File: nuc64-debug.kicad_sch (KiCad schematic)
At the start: 12 parts, among them J1 SWD, J2 POW, SW1 BOOT, SW2 RST

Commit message: Fixed trace width
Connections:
- net VBUS: now reaches DBG1.9 (Pin_9), J2.3 (Pin_3)
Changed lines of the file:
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@@
+	)
+	(junction
+		(at 152.4 35.56)
+		(diameter 0)
+		(color 0 0 0 0)
 	)
 	(junction
@@
 	(wire
 		(pts
+			(xy 171.45 35.56) (xy 171.45 27.94)
+		)
+		(stroke
+			(width 0)
+			(type default)
+		)
+	)
+	(wire
+		(pts
 			(xy 154.94 73.66) (xy 154.94 81.28)
 		)
@@
 		(pts
 			(xy 180.34 130.81) (xy 165.1 130.81)
+		)
+		(stroke
+			(width 0)
+			(type default)
+		)
+	)
+	(wire
+		(pts
+			(xy 152.4 35.56) (xy 171.45 35.56)
 		)
 		(stroke
@@
 					(unit 1)
 				)
+			)
+		)
+	)
+	(symbol
+		(lib_id "power:VBUS")
+		(at 171.45 27.94 0)
+		(unit 1)
+		(exclude_from_sim no)
+		(in_bom yes)
+		(on_board yes)
+		(dnp no)
+		(fields_autoplaced yes)
+		(property "Reference" "#PWR02"
+			(at 171.45 31.75 0)
+			(effects
+				(font
+					(size 1.27 1.27)
+				)
+				(hide yes)
+			)
+		)
+		(property "Value" "VBUS"
+			(at 171.45 22.86 0)
+			(effects
+				(font
+					(size 1.27 1.27)
+				)
+			)
+		)
+		(property "Footprint" ""
+			(at 171.45 27.94 0)
+			(effects
+				(font
+					(size 1.27 1.27)
+				)
+				(hide yes)
+			)
+		)
+		(property "Datasheet" ""
+			(at 171.45 27.94 0)
+			(effects
+				(font
+					(size 1.27 1.27)
+				)
+				(hide yes)
+			)
+		)
+		(property "Description" "Power symbol creates a global label with name \"VBUS\""
+			(at 171.45 27.94 0)
+			(effects
+				(font
+					(size 1.27 1.27)
+				)
+				(hide yes)
+			)
+		)
+		(pin "1"
+		)
+		(instances
+			(project ""
+				(path "/12c2bc1e-4869-4a56-bffb-ffa29b2d4bba"
+					(reference "#PWR02")
+					(unit 1)
+				)

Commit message: Shrink
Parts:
- added C3: 10n, Capacitor_SMD:C_0603_1608Metric, symbol Device:C
- added C4: 10µ, Capacitor_SMD:C_0603_1608Metric, symbol Device:C
- added C5: 100n, Capacitor_SMD:C_0603_1608Metric, symbol Device:C
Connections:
- net GND: now also C3.2, C4.2, C5.2
- net VDD: now also C3.1, C4.1, C5.1

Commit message: Added UART LEDs
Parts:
- added D2: RX, LED_SMD:LED_0603_1608Metric, symbol Device:LED
- added D3: TX, LED_SMD:LED_0603_1608Metric, symbol Device:LED
- added R4, R5: 1K, Resistor_SMD:R_0603_1608Metric, symbol Device:R
- added R6, R7: 680, Resistor_SMD:R_0603_1608Metric, symbol Device:R
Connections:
- net VDD: now also D2.2 (A), D3.2 (A), R4.2, R5.2
- net at DBG1.7 (Pin_7), UART1.2 (Pin_2): now also R5.1, R7.2
- net at DBG1.8 (Pin_8), UART1.1 (Pin_1): now also R4.1, R6.2
- new net: D3.1 (K), R7.1
- new net: D2.1 (K), R6.1
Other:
- moved on the sheet: C1, C3, C4, C5, D1, R2, R3, SW2

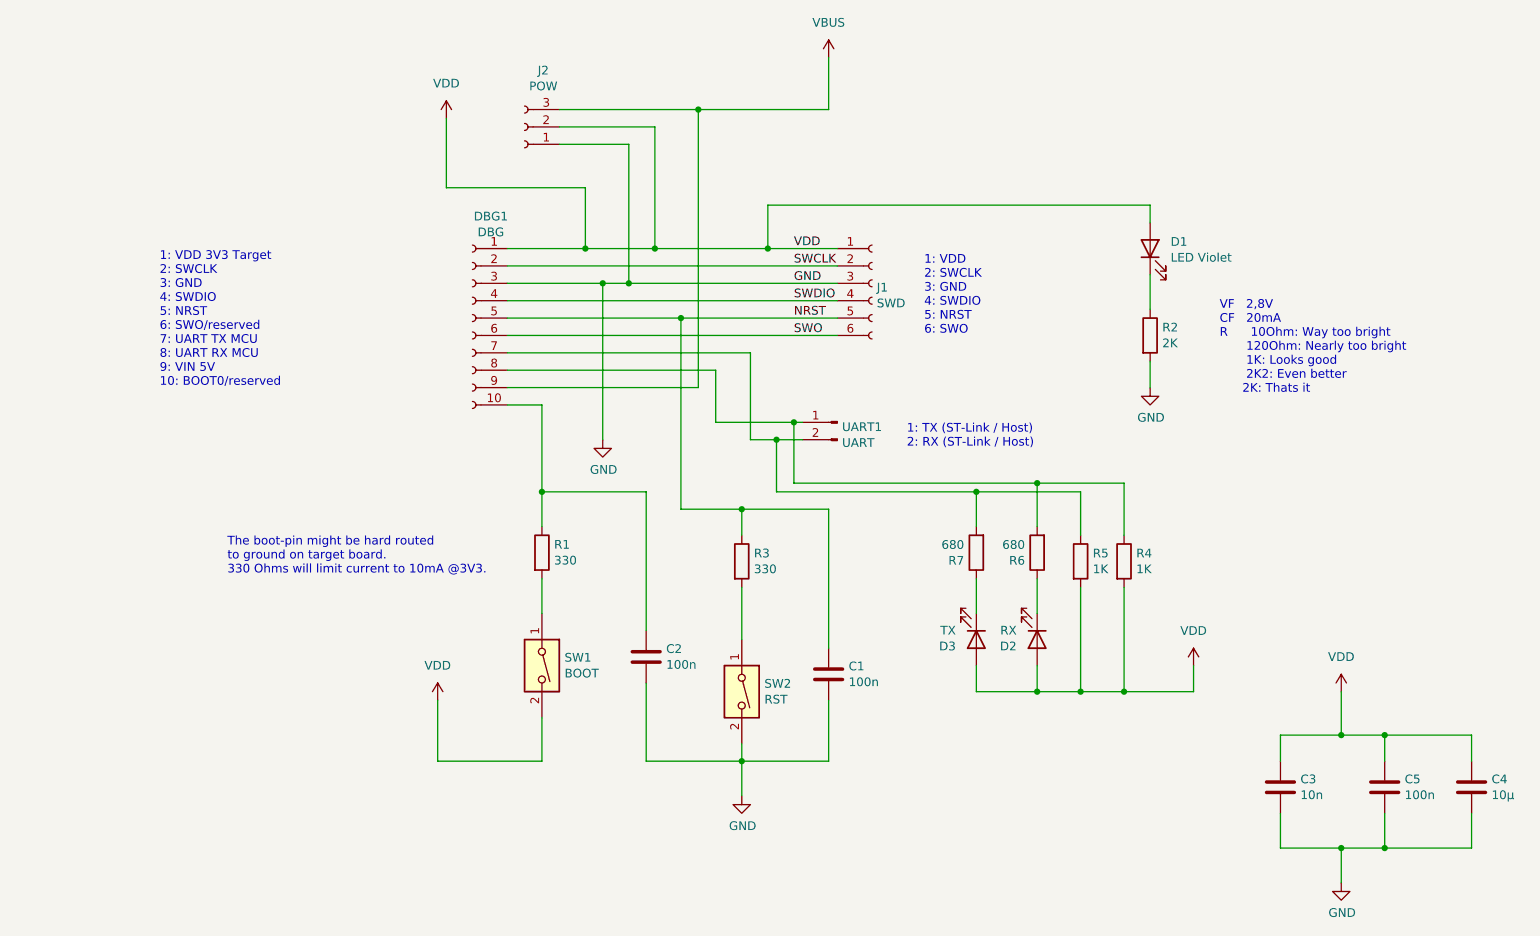
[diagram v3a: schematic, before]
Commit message: Added mounting hole for soldering
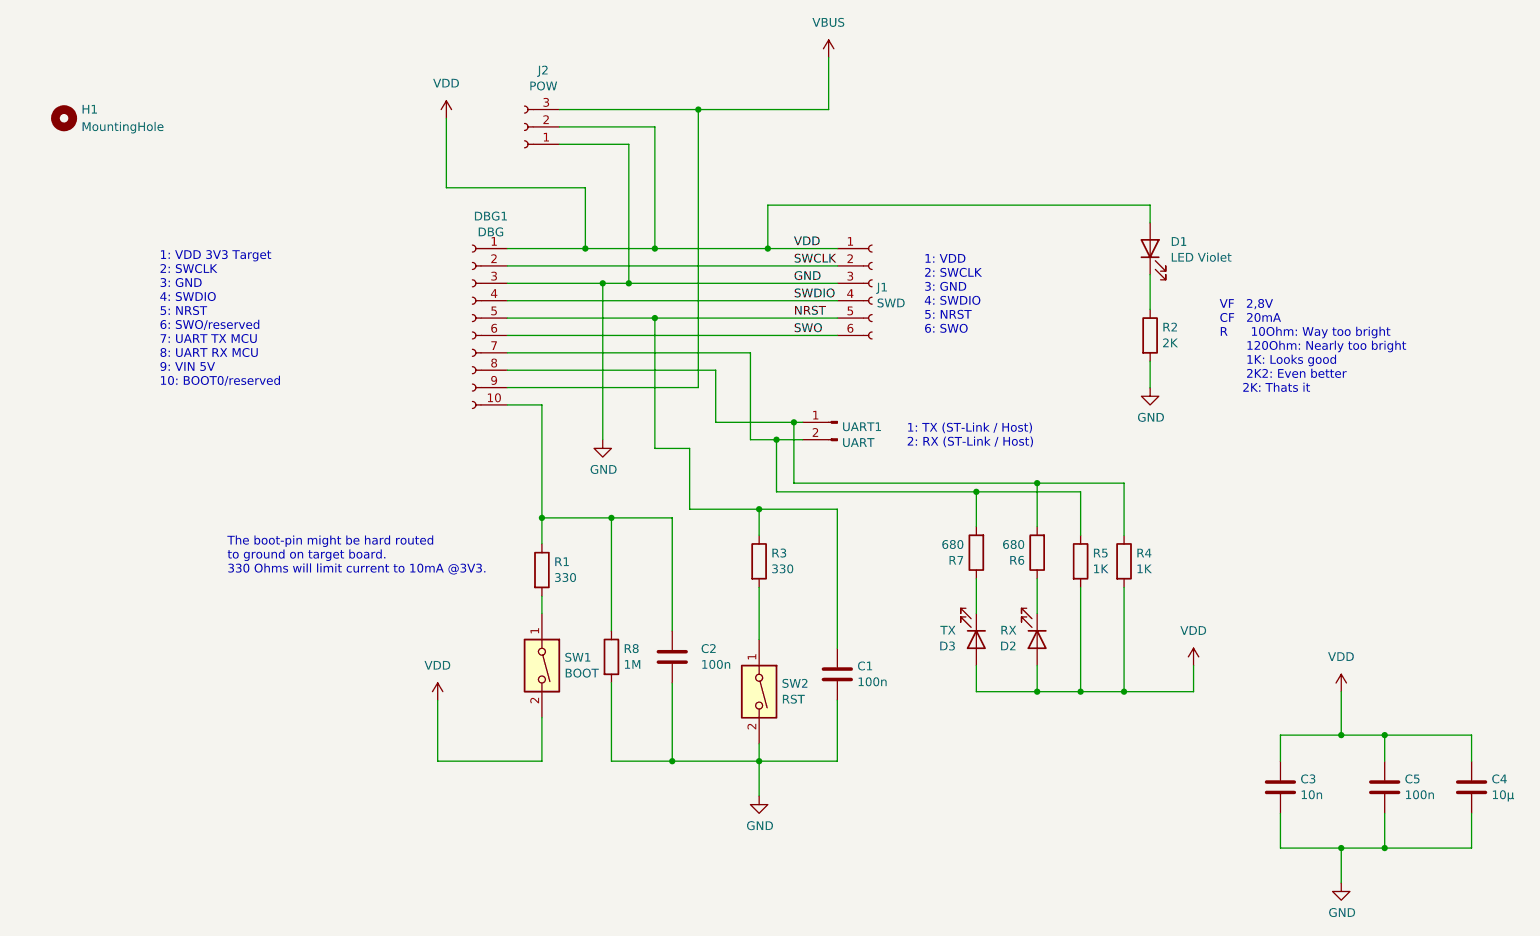
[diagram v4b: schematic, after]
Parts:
- added H1: MountingHole, MountingHole:MountingHole_2.2mm_M2_DIN965, symbol Mechanical:MountingHole
- added R8: 1M, Resistor_SMD:R_0603_1608Metric, symbol Device:R
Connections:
- net GND: now also R8.2
- net at C2.1, DBG1.10 (Pin_10), R1.1: now also R8.1
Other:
- moved on the sheet: C1, C2, R1, R3, SW2

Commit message: Made UART pullups optional
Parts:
- R4, R5: value 1K -> OPT_1K; now not fitted
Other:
- note added: "Already pulled high on Nucleo board. No resistor found. Could be internal pullup of STLink."
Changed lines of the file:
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@@
 		)
 	)
+	(text "Already pulled high on Nucleo board.\nNo resistor found. Could be internal pullup\nof STLink."
+		(exclude_from_sim no)
+		(at 243.586 102.87 0)
+		(effects
+			(font
+				(size 1.27 1.27)
+			)
+		)
+	)
 	(junction
 		(at 163.83 83.82)
@@
 		(in_bom yes)
 		(on_board yes)
-		(dnp no)
+		(dnp yes)
 		(property "Reference" "R4"
 			(at 216.408 100.4316 0)
@@
 			)
 		)
-		(property "Value" "1K"
-			(at 216.408 102.743 0)
+		(property "Value" "OPT_1K"
+			(at 217.678 108.966 90)
 			(effects
 				(font
@@
 		(in_bom yes)
 		(on_board yes)
-		(dnp no)
+		(dnp yes)
 		(property "Reference" "R5"
 			(at 210.058 100.4316 0)
@@
 			)
 		)
-		(property "Value" "1K"
-			(at 210.058 102.743 0)
+		(property "Value" "OPT_1K"
+			(at 211.328 109.22 90)
 			(effects
 				(font

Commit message: Updated values for R6/R7
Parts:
- R6, R7: value 680 -> 51
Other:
- note added: "R6/R7: (3-2)/0,02=50 Ohm Single keypresses are barely noticable on LEDs due to small impulses. Dont make resistor too high (680Ohm way too high). So the LEDs are a little bit useless."
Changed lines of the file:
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@@
+		)
+	)
+	(text "R6/R7: (3-2)/0,02=50 Ohm\nSingle keypresses are barely noticable \non LEDs due to small impulses.\nDont make resistor too high (680Ohm way \ntoo high).\nSo the LEDs are a little bit useless."
+		(exclude_from_sim no)
+		(at 182.372 132.334 0)
+		(effects
+			(font
+				(size 1.27 1.27)
+			)
+			(justify left)
 		)
 	)
@@
 			)
 		)
-		(property "Value" "680"
+		(property "Value" "51"
 			(at 200.152 99.187 0)
 			(effects
@@
 			)
 		)
-		(property "Value" "680"
+		(property "Value" "51"
 			(at 191.262 99.187 0)
 			(effects
